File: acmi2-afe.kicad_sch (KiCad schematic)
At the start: 14 parts

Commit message: push from windows
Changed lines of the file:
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@@
+	(bus
+		(pts
+			(xy 144.78 94.615) (xy 151.13 94.615)
+		)
+		(stroke
+			(width 0)
+			(type default)
+		)
+	)
+	(wire
+		(pts
+			(xy 346.71 187.96) (xy 346.71 186.69)
+		)
+		(stroke
+			(width 0)
+			(type default)
+		)
+	)
+	(wire
+		(pts
+			(xy 373.38 208.28) (xy 373.38 207.01)
+		)
+		(stroke
+			(width 0)
+			(type default)
+		)
+	)
+	(wire
+		(pts
+			(xy 214.63 87.63) (xy 237.49 87.63)
+		)
+		(stroke
+			(width 0)
+			(type default)
+		)
+	)
+	(bus
+		(pts
+			(xy 151.13 94.615) (xy 151.13 95.25)
+		)
+		(stroke
+			(width 0)
+			(type default)
+		)
+	)
+	(wire
+		(pts
+			(xy 156.21 171.45) (xy 175.26 171.45)
+		)
+		(stroke
+			(width 0)
+			(type default)
+		)
+	)
+	(wire
+		(pts
+			(xy 387.35 208.28) (xy 387.35 207.01)
+		)
+		(stroke
+			(width 0)
+			(type default)
+		)
+	)
+	(wire
+		(pts
+			(xy 316.23 187.96) (xy 316.23 186.69)
+		)
+		(stroke
+			(width 0)
+			(type default)
+		)
+	)
+	(bus
+		(pts
+			(xy 151.13 130.81) (xy 175.26 130.81)
+		)
+		(stroke
+			(width 0)
+			(type default)
+		)
+	)
+	(wire
+		(pts
+			(xy 359.41 208.28) (xy 359.41 207.01)
+		)
+		(stroke
+			(width 0)
+			(type default)
+		)
+	)
 	(bus
 		(pts
@@
 	(wire
 		(pts
-			(xy 346.71 187.96) (xy 346.71 186.69)
+			(xy 355.6 187.96) (xy 355.6 186.69)
 		)
 		(stroke
@@
 		)
 	)
-	(wire
+	(bus
 		(pts
-			(xy 373.38 208.28) (xy 373.38 207.01)
+			(xy 214.63 161.29) (xy 237.49 161.29)
 		)
 		(stroke
@@
 	(wire
 		(pts
-			(xy 214.63 87.63) (xy 237.49 87.63)
+			(xy 330.2 208.28) (xy 330.2 207.01)
 		)
 		(stroke
@@
 	(wire
 		(pts
-			(xy 156.21 171.45) (xy 175.26 171.45)
+			(xy 344.17 208.28) (xy 344.17 207.01)
 		)
 		(stroke
@@
 	(wire
 		(pts
-			(xy 387.35 208.28) (xy 387.35 207.01)
+			(xy 365.76 187.96) (xy 365.76 186.69)
 		)
 		(stroke
@@
 	(wire
 		(pts
-			(xy 316.23 187.96) (xy 316.23 186.69)
+			(xy 386.08 187.96) (xy 386.08 186.69)
 		)
 		(stroke
@@
 		)
 	)
-	(bus
+	(wire
 		(pts
-			(xy 151.13 130.81) (xy 175.26 130.81)
+			(xy 326.39 187.96) (xy 326.39 186.69)
 		)
 		(stroke
@@
 	(wire
 		(pts
-			(xy 359.41 208.28) (xy 359.41 207.01)
+			(xy 336.55 187.96) (xy 336.55 186.69)
 		)
 		(stroke
@@
 		)
 	)
-	(wire
+	(bus
 		(pts
-			(xy 355.6 187.96) (xy 355.6 186.69)
+			(xy 214.63 120.65) (xy 237.49 120.65)
 		)
 		(stroke
@@
 		)
 	)
-	(bus
-		(pts
-			(xy 214.63 161.29) (xy 237.49 161.29)
-		)
-		(stroke
-			(width 0)
-			(type default)
-		)
-	)
-	(wire
-		(pts
-			(xy 330.2 208.28) (xy 330.2 207.01)
-		)
-		(stroke
-			(width 0)
-			(type default)
-		)
-	)
-	(wire
-		(pts
-			(xy 344.17 208.28) (xy 344.17 207.01)
-		)
-		(stroke
-			(width 0)
-			(type default)
-		)
-	)
-	(wire
-		(pts
-			(xy 365.76 187.96) (xy 365.76 186.69)
-		)
-		(stroke
-			(width 0)
-			(type default)
-		)
-	)
-	(wire
-		(pts
-			(xy 386.08 187.96) (xy 386.08 186.69)
-		)
-		(stroke
-			(width 0)
-			(type default)
-		)
-	)
-	(wire
-		(pts
-			(xy 326.39 187.96) (xy 326.39 186.69)
-		)
-		(stroke
-			(width 0)
-			(type default)
-		)
-	)
-	(wire
-		(pts
-			(xy 336.55 187.96) (xy 336.55 186.69)
-		)
-		(stroke
-			(width 0)
-			(type default)
-		)
-	)
-	(bus
-		(pts
-			(xy 214.63 120.65) (xy 237.49 120.65)
-		)
-		(stroke
-			(width 0)
-			(type default)
-		)
-	)
 	(symbol
 		(lib_id "Connector:TestPoint")
@@
 	)
 	(sheet
-		(at 124.46 81.915)
+		(at 118.11 81.28)
 		(size 26.67 26.67)
 		(exclude_from_sim no)
@@
 		)
 		(property "Sheetname" "adc"
-			(at 124.46 81.2034 0)
+			(at 118.11 80.5684 0)
 			(effects
 				(font
@@
 		)
 		(property "Sheetfile" "adc.kicad_sch"
-			(at 124.46 109.1696 0)
+			(at 118.11 108.5346 0)
 			(effects
 				(font
@@
 		)
 		(pin "{ADC}" bidirectional
-			(at 151.13 95.25 0)
-			(effects
-				(font
+			(at 144.78 94.615 0)
+			(effects
+				(font

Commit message: Finish routing
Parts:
- removed TP5, TP6: ${SHORT_NET_NAME(1)}, My Footprints:TestPoint_RCS-0C, symbol Connector:TestPoint

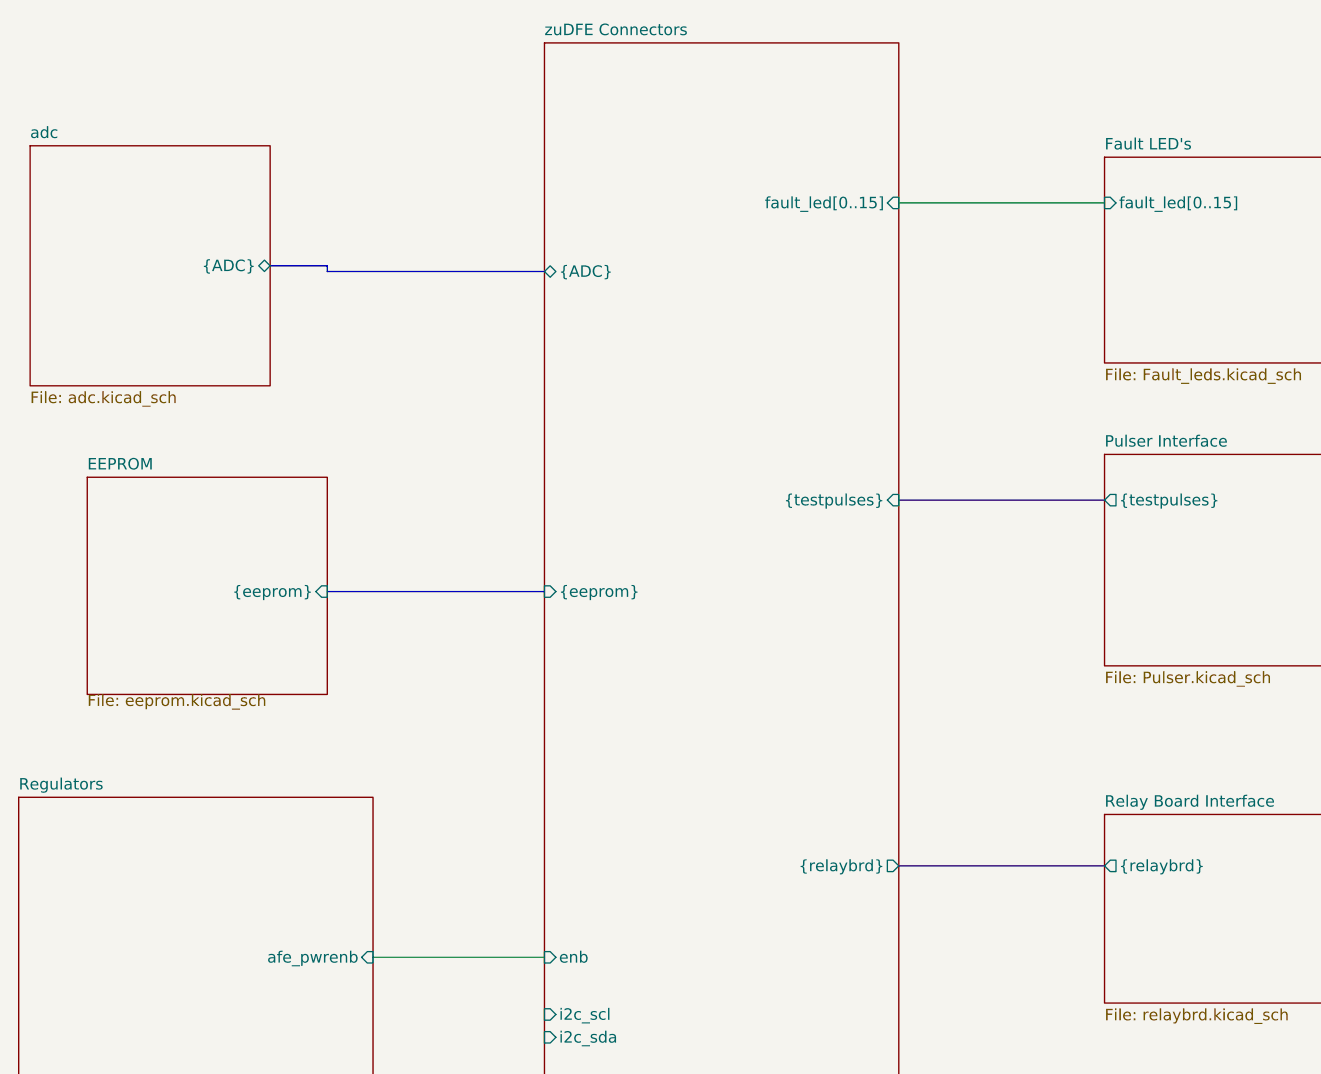
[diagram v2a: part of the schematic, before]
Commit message: Add watchdog window IC
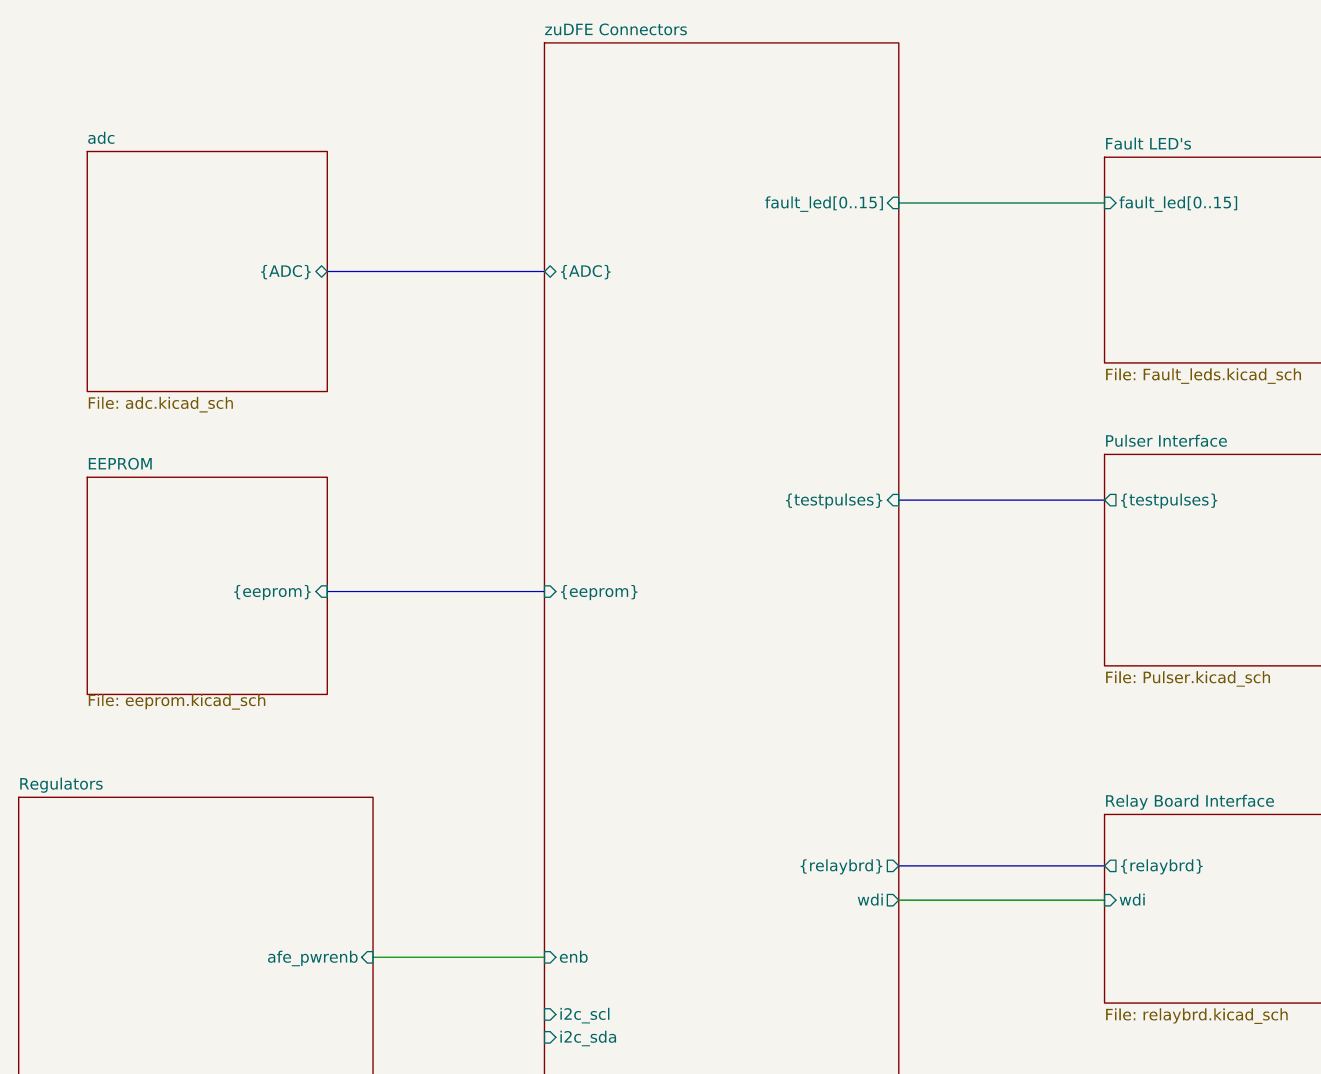
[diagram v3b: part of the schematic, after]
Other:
- sheet Relay Board Interface ports: added wdi; removed none
- sheet zuDFE Connectors ports: added wdi; removed none
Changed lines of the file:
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@@
 		)
 	)
-	(bus
+	(wire
 		(pts
-			(xy 144.78 94.615) (xy 151.13 94.615)
+			(xy 346.71 187.96) (xy 346.71 186.69)
 		)
 		(stroke
@@
 	(wire
 		(pts
-			(xy 346.71 187.96) (xy 346.71 186.69)
+			(xy 214.63 87.63) (xy 237.49 87.63)
 		)
 		(stroke
@@
 	(wire
 		(pts
-			(xy 214.63 87.63) (xy 237.49 87.63)
+			(xy 156.21 171.45) (xy 175.26 171.45)
 		)
 		(stroke
@@
 		)
 	)
-	(bus
+	(wire
 		(pts
-			(xy 151.13 94.615) (xy 151.13 95.25)
+			(xy 316.23 187.96) (xy 316.23 186.69)
 		)
 		(stroke
@@
 		)
 	)
-	(wire
+	(bus
 		(pts
-			(xy 156.21 171.45) (xy 175.26 171.45)
+			(xy 151.13 130.81) (xy 175.26 130.81)
 		)
 		(stroke
@@
 	(wire
 		(pts
-			(xy 316.23 187.96) (xy 316.23 186.69)
+			(xy 359.41 208.28) (xy 359.41 207.01)
 		)
 		(stroke
@@
 	(bus
 		(pts
-			(xy 151.13 130.81) (xy 175.26 130.81)
+			(xy 151.13 95.25) (xy 175.26 95.25)
 		)
 		(stroke
@@
 	(wire
 		(pts
-			(xy 359.41 208.28) (xy 359.41 207.01)
+			(xy 355.6 187.96) (xy 355.6 186.69)
 		)
 		(stroke
@@
 	(bus
 		(pts
-			(xy 151.13 95.25) (xy 175.26 95.25)
+			(xy 214.63 161.29) (xy 237.49 161.29)
 		)
 		(stroke
@@
 	(wire
 		(pts
-			(xy 355.6 187.96) (xy 355.6 186.69)
+			(xy 330.2 208.28) (xy 330.2 207.01)
 		)
 		(stroke
@@
 		)
 	)
-	(bus
+	(wire
 		(pts
-			(xy 214.63 161.29) (xy 237.49 161.29)
+			(xy 344.17 208.28) (xy 344.17 207.01)
 		)
 		(stroke
@@
 	(wire
 		(pts
-			(xy 330.2 208.28) (xy 330.2 207.01)
+			(xy 214.63 165.1) (xy 237.49 165.1)
 		)
 		(stroke
@@
 	(wire
 		(pts
-			(xy 344.17 208.28) (xy 344.17 207.01)
+			(xy 365.76 187.96) (xy 365.76 186.69)
 		)
 		(stroke
@@
 	(wire
 		(pts
-			(xy 365.76 187.96) (xy 365.76 186.69)
+			(xy 386.08 187.96) (xy 386.08 186.69)
 		)
 		(stroke
@@
 	(wire
 		(pts
-			(xy 386.08 187.96) (xy 386.08 186.69)
+			(xy 326.39 187.96) (xy 326.39 186.69)
 		)
 		(stroke
@@
 	(wire
 		(pts
-			(xy 326.39 187.96) (xy 326.39 186.69)
+			(xy 336.55 187.96) (xy 336.55 186.69)
 		)
 		(stroke
@@
 		)
 	)
-	(wire
+	(bus
 		(pts
-			(xy 336.55 187.96) (xy 336.55 186.69)
+			(xy 214.63 120.65) (xy 237.49 120.65)
 		)
 		(stroke
@@
 		)
 	)
-	(bus
-		(pts
-			(xy 214.63 120.65) (xy 237.49 120.65)
-		)
-		(stroke
-			(width 0)
-			(type default)
-		)
-	)
 	(symbol
 		(lib_id "Mechanical:MountingHole_Pad")
@@
 	)
 	(sheet
-		(at 118.11 81.28)
+		(at 124.46 81.915)
 		(size 26.67 26.67)
 		(exclude_from_sim no)
@@
 		)
 		(property "Sheetname" "adc"
-			(at 118.11 80.5684 0)
+			(at 124.46 81.2034 0)
 			(effects
 				(font
@@
 		)
 		(property "Sheetfile" "adc.kicad_sch"
-			(at 118.11 108.5346 0)
+			(at 124.46 109.1696 0)
 			(effects
 				(font
@@
 		)
 		(pin "{ADC}" bidirectional
-			(at 144.78 94.615 0)
+			(at 151.13 95.25 0)
 			(effects
 				(font
@@
 			)
 		)
+		(pin "wdi" output
+			(at 214.63 165.1 0)
+			(effects
+				(font
+					(size 1.27 1.27)
+				)
+				(justify right)
+			)
+		)
 		(instances
 			(project "acmi2-afe"
@@
 			(effects
 				(font
+					(size 1.27 1.27)
+				)
+				(justify left)
+			)
+		)
+		(pin "wdi" input
+			(at 237.49 165.1 180)
+			(effects
+				(font

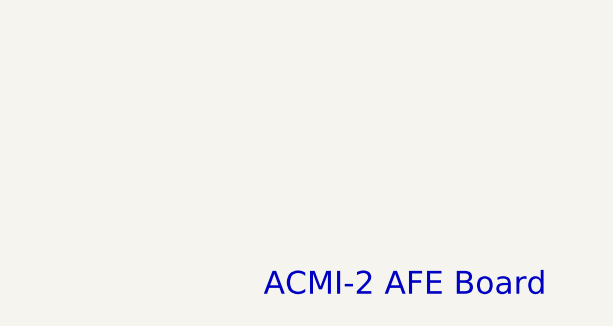
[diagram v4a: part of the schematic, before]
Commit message: Add drawing borders, moved copper pours inside board edge, add fab notes, update bnl logo
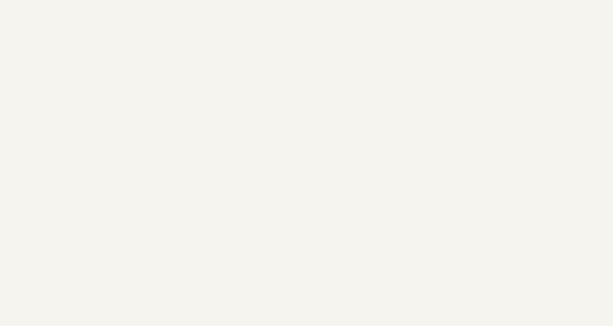
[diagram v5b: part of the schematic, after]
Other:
- note removed: "ACMI-2 AFE Board"

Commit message: Nightly commit
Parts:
- TP1, TP2, TP3, TP4: value ${SHORT_NET_NAME(1)} -> GND
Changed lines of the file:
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@@
 			)
 		)
-		(property "Value" "${SHORT_NET_NAME(1)}"
+		(property "Value" "GND"
 			(at 318.77 204.9779 0)
 			(effects
@@
 			)
 		)
-		(property "Value" "${SHORT_NET_NAME(1)}"
+		(property "Value" "GND"
 			(at 332.74 204.9779 0)
 			(effects
@@
 			)
 		)
-		(property "Value" "${SHORT_NET_NAME(1)}"
+		(property "Value" "GND"
 			(at 361.95 204.9779 0)
 			(effects
@@
 			)
 		)
-		(property "Value" "${SHORT_NET_NAME(1)}"
+		(property "Value" "GND"
 			(at 346.71 204.9779 0)
 			(effects
